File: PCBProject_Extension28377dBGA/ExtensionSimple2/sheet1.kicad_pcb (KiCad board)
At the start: 4 copper layers, 122.2 x 108.4 mm, 114 parts, among them J1 Conn_02x05_Odd_Even, J2 Conn_01x02_Pin, J3 Conn_01x02_Pin, J4 CAN_1_CONNECT, J5 RS485_1_CONNECT, J6 CAN_2_CONNECT, J7 RS485_2_CONNECT, Q1 FMMT618TA, U1 SN74ABT541, U2 SN74ABT541, U4 SN65HVD230, U5 SN65HVD230

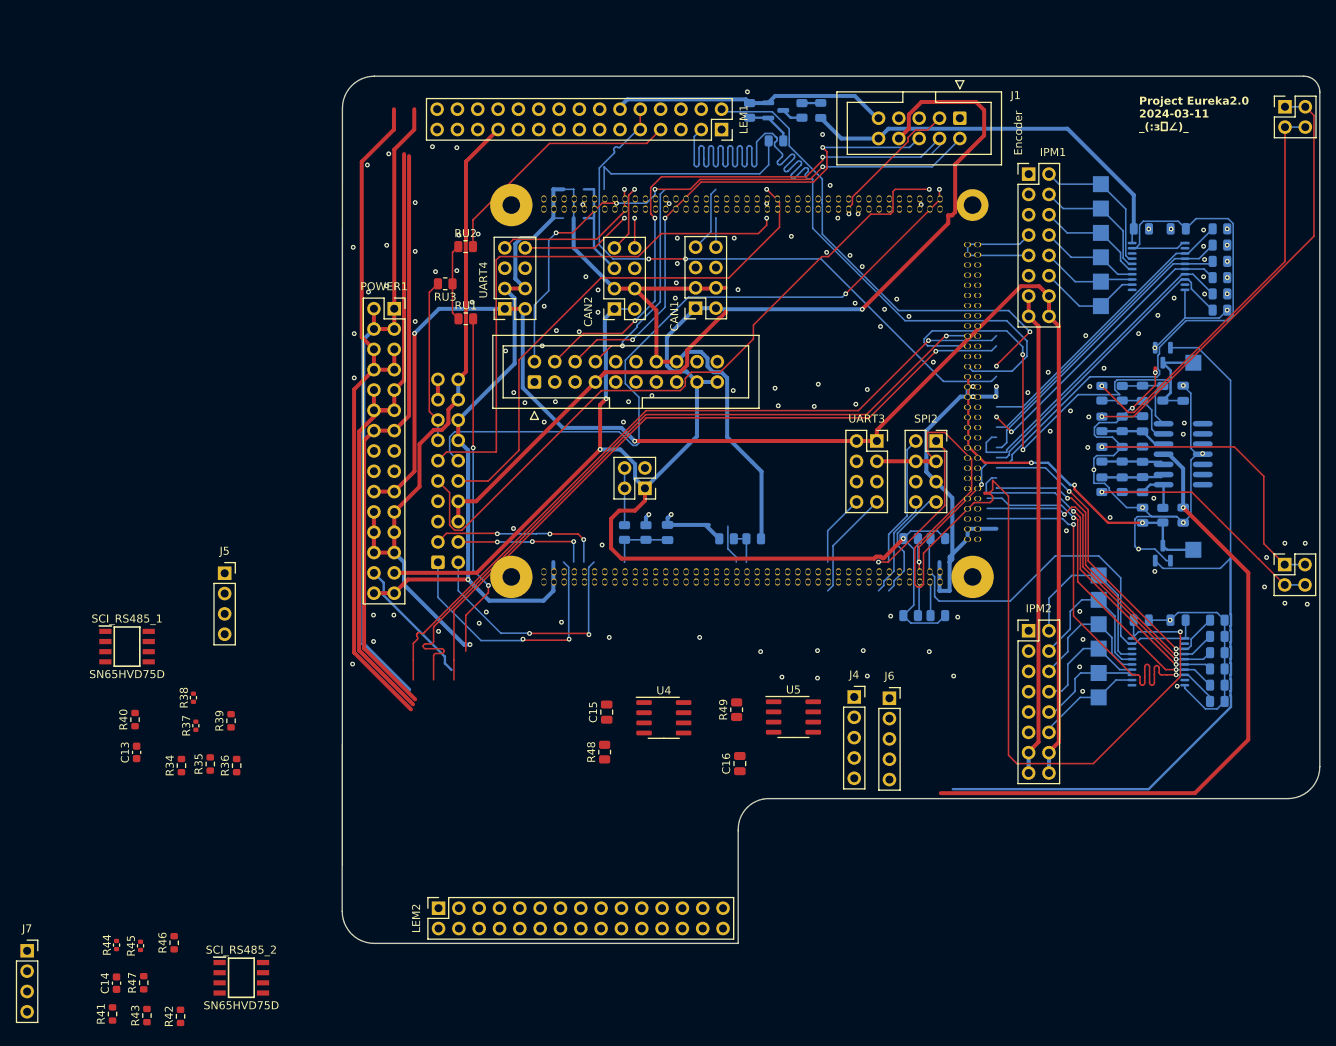
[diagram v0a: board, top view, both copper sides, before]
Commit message: 确定底板尺寸，目前只差布线
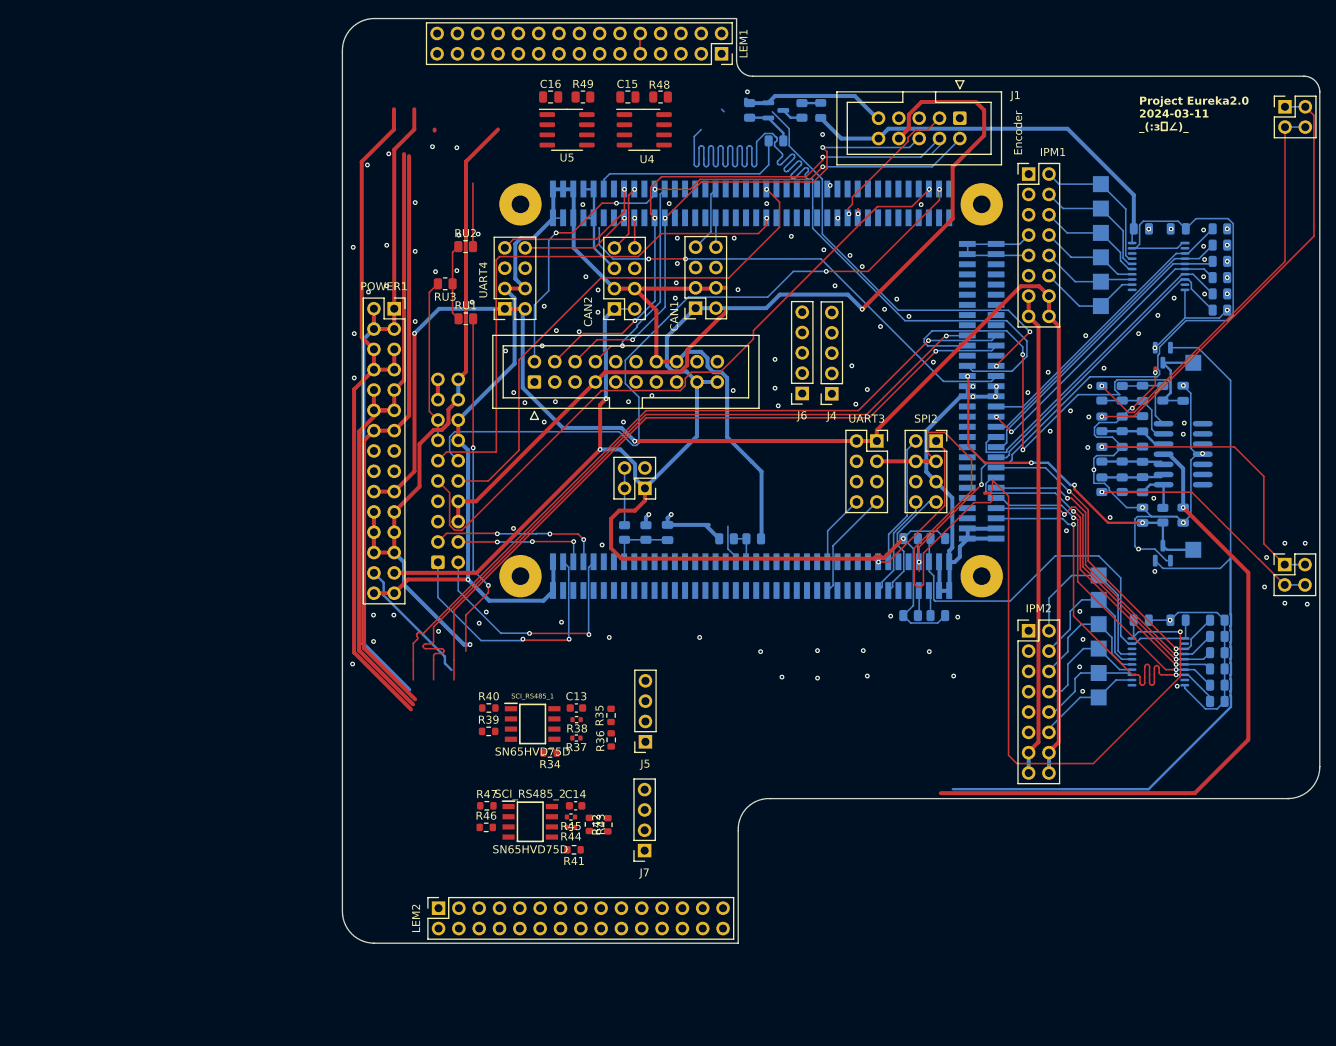
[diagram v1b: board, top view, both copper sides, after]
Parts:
- DSP1: footprint Oshinoko:DSP_240_0p6mm -> 1mmlab_pcb_lib:DSP_240_SMD
- moved C16 86.6 mm to (217.8, 76.6), turned to 180 degrees
- moved R48 82.2 mm to (231.6, 76.6), turned to 180 degrees
- moved R49 79.0 mm to (221.9, 76.6), turned to 180 degrees
- moved U5 78.7 mm to (219.9, 80.7)
- moved J7 78.2 mm to (229.6, 170.8), turned to 180 degrees
- moved C15 76.9 mm to (227.5, 76.6), turned to 180 degrees
- moved U4 73.5 mm to (229.6, 80.7)
- moved C14 61.5 mm to (221.0, 165.2), turned to 0 degrees
- moved R41 61.2 mm to (220.8, 170.7), turned to 180 degrees
- moved R43 60.3 mm to (222.7, 167.5), turned to -90 degrees
- moved R44 58.7 mm to (220.4, 167.9), turned to 180 degrees
- moved R42 58.5 mm to (225.0, 167.6)
- moved J5 56.7 mm to (229.7, 157.2), turned to 180 degrees
- moved R45 56.2 mm to (220.4, 166.6), turned to 180 degrees
- moved C13 55.3 mm to (221.1, 153.0), turned to 0 degrees
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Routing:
- net AGND: track 318.7 -> 232.2 mm, vias 144 -> 142
- net /IPM_IU1: track 0.00 -> 59.2 mm, vias 0 -> 2
- net Net-(LEM1-Pad7): track 31.5 -> 7.94 mm
- net /IPM_IW1: track 61.4 -> 55.4 mm
- net /SPI_A_MO_HS: track 87.0 -> 85.1 mm
- net /LED1: track 27.2 -> 25.6 mm
- net VDD: track 232.0 -> 233.2 mm
- net /DSP_PWM3~{_ENABL}E: track 4.32 -> 3.21 mm
- net /DSP_PWM4~{_ENABL}E: track 4.32 -> 3.22 mm
- net /DSP-PWM6A: track 40.6 -> 39.5 mm
- net /DSP-PWM5B: track 42.1 -> 41.0 mm
- net /DSP-PWM6B: track 53.1 -> 52.0 mm
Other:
- board size 122.2 x 108.4 mm -> 122.2 x 115.6 mm

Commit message: 底板布线基本完毕，但是还有些地方出现了混乱，仍需改进
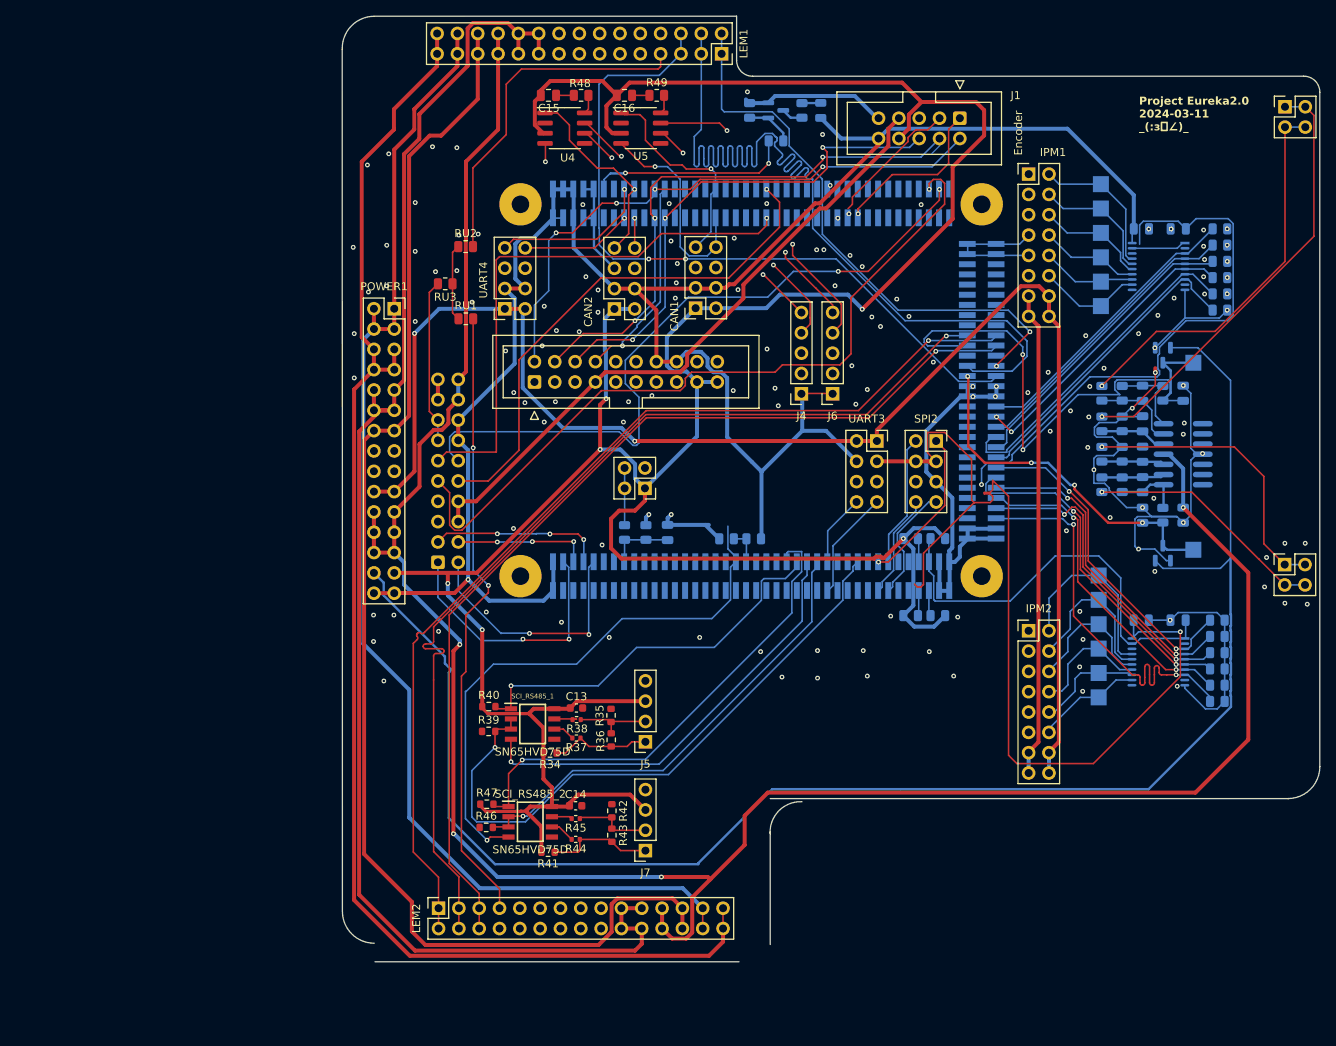
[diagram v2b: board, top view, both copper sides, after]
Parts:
- moved C15 9.93 mm to (217.6, 76.4), turned to 0 degrees
- moved R48 9.93 mm to (221.7, 76.4)
- moved U4 9.93 mm to (219.6, 80.5)
- moved R49 9.23 mm to (231.1, 76.4)
- moved C16 9.23 mm to (227.1, 76.4), turned to 0 degrees
- moved U5 9.23 mm to (229.1, 80.5)
- moved J6 3.80 mm to (253.1, 113.7)
- moved J4 3.80 mm to (249.2, 113.7)
- moved R41 3.26 mm to (217.5, 171.0)
- moved R43 3.11 mm to (225.5, 168.9)
- moved R42 1.82 mm to (225.5, 165.8), turned to -90 degrees
- moved R44 1.62 mm to (221.0, 169.4)
- moved R45 0.63 mm to (221.0, 166.8)
- moved R47 0.20 mm to (209.9, 165.0)
- moved R40 0.17 mm to (210.1, 152.8)
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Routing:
- net VDD: track 233.2 -> 378.9 mm, vias 4 -> 6
- net A+5V: track 164.0 -> 283.7 mm, vias 2 -> 4
- net 12VGND: track 80.0 -> 182.9 mm
- net A-5V: track 74.4 -> 165.0 mm
- net AVDD: track 115.8 -> 203.8 mm
- net -12: track 86.5 -> 172.9 mm
- net /DSP_PWM1~{_ENABL}E: track 96.1 -> 10.4 mm, vias 2 -> 0
- net /UART_WRA: track 0.00 -> 78.9 mm, vias 0 -> 1
- net +12: track 81.6 -> 153.2 mm
- net unconnected-(C1-Pad2): track 0.00 -> 70.9 mm, vias 0 -> 1
- net /UART_SCI_TXDB: track 4.92 -> 70.4 mm, vias 0 -> 1
- net /UART_SCI_RXDB: track 0.00 -> 61.0 mm, vias 0 -> 1
- net /UART_WRB: track 0.00 -> 59.0 mm, vias 0 -> 1
- net /UART_SCI_TXDA: track 0.00 -> 54.4 mm, vias 0 -> 1
- net /UART_SCI_RXDA: track 0.00 -> 48.1 mm, vias 0 -> 1
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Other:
- board size 122.2 x 115.6 mm -> 122.2 x 118.2 mm

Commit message: 底板布线完毕！
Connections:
- C1 pad 1: unconnected-(C1-Pad1) -> AGND
- C1 pad 2: unconnected-(C1-Pad2) -> /DSP_PWM1~{_ENABL}E
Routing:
- net /DSP_PWM1~{_ENABL}E: track 10.4 -> 85.8 mm, vias 0 -> 2
- net unconnected-(C1-Pad2): track 70.9 -> 0.00 mm, vias 1 -> 0
- net AGND: track 234.1 -> 257.4 mm, vias 141 -> 152
- net D+5V: track 397.1 -> 375.6 mm
- net /IPM_IU2: track 123.1 -> 137.4 mm
- net /QEP1_HALL_W: track 70.1 -> 62.1 mm
- net /IPM_IV1: track 127.0 -> 119.5 mm
- net /IPM_VDC_BUS2: track 71.0 -> 66.1 mm
- net /UART_SCI_TXDB: track 70.4 -> 66.8 mm
- net /CAN_1L: track 36.4 -> 39.6 mm
- net AVDD: track 203.8 -> 206.7 mm
- net /CAN_1H: track 41.8 -> 44.2 mm
- net A+5V: track 283.7 -> 281.8 mm
- net /QEP1_HALL_U: track 71.0 -> 69.3 mm
- net VDD: track 378.9 -> 377.6 mm
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- added copper zone on In1.Cu, net AGND
- added copper zone on In2.Cu, net AGND
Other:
- board size 122.2 x 118.2 mm -> 122.2 x 118.3 mm
- board text added: "CAN_1_CONNECT"
- board text added: "CAN_2_CONNECT"
- board text added: "Project Eureka2.0 2024-03-23 _(:з」∠)_"
- board text added: "RS485_1"
- board text added: "RS485_2"
- board text removed: "Project Eureka2.0 2024-03-11 _(:з」∠)_"
